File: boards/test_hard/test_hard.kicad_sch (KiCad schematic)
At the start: 12 parts, among them IC1 ADS114S08BIPBS, U2 ESP32-S3-MINI-1

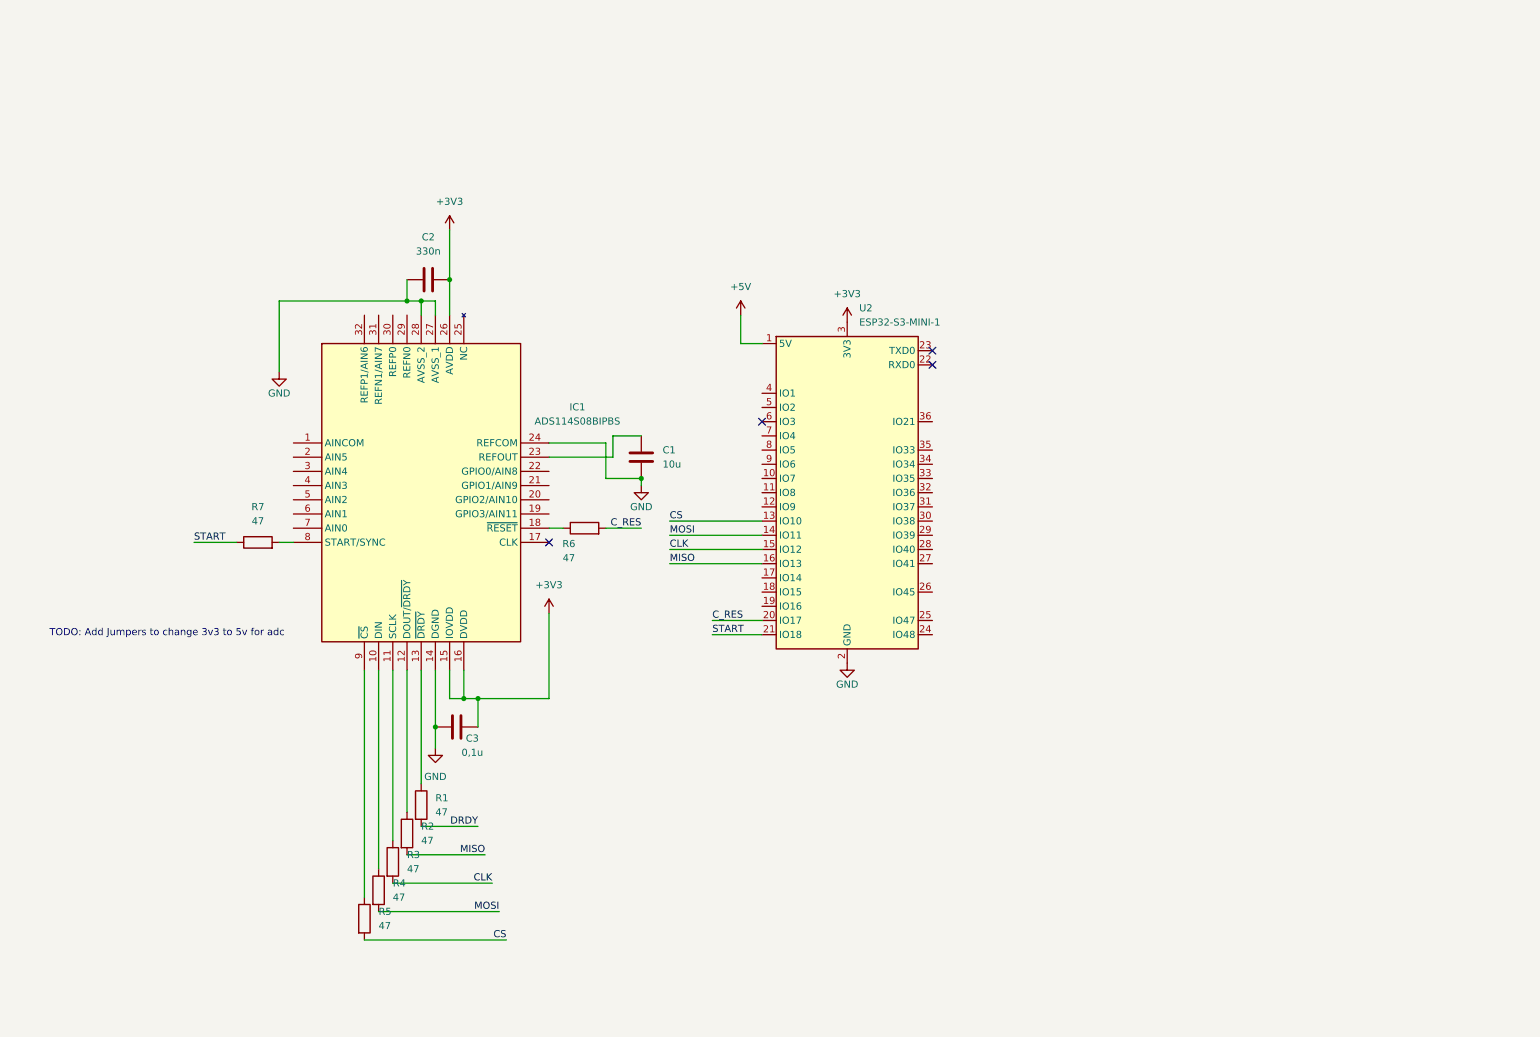
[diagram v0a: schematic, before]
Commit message: Test Hardware Board
Still missing CAN

Signed-off-by: Philipp Macher <philipp-macher@web.de>
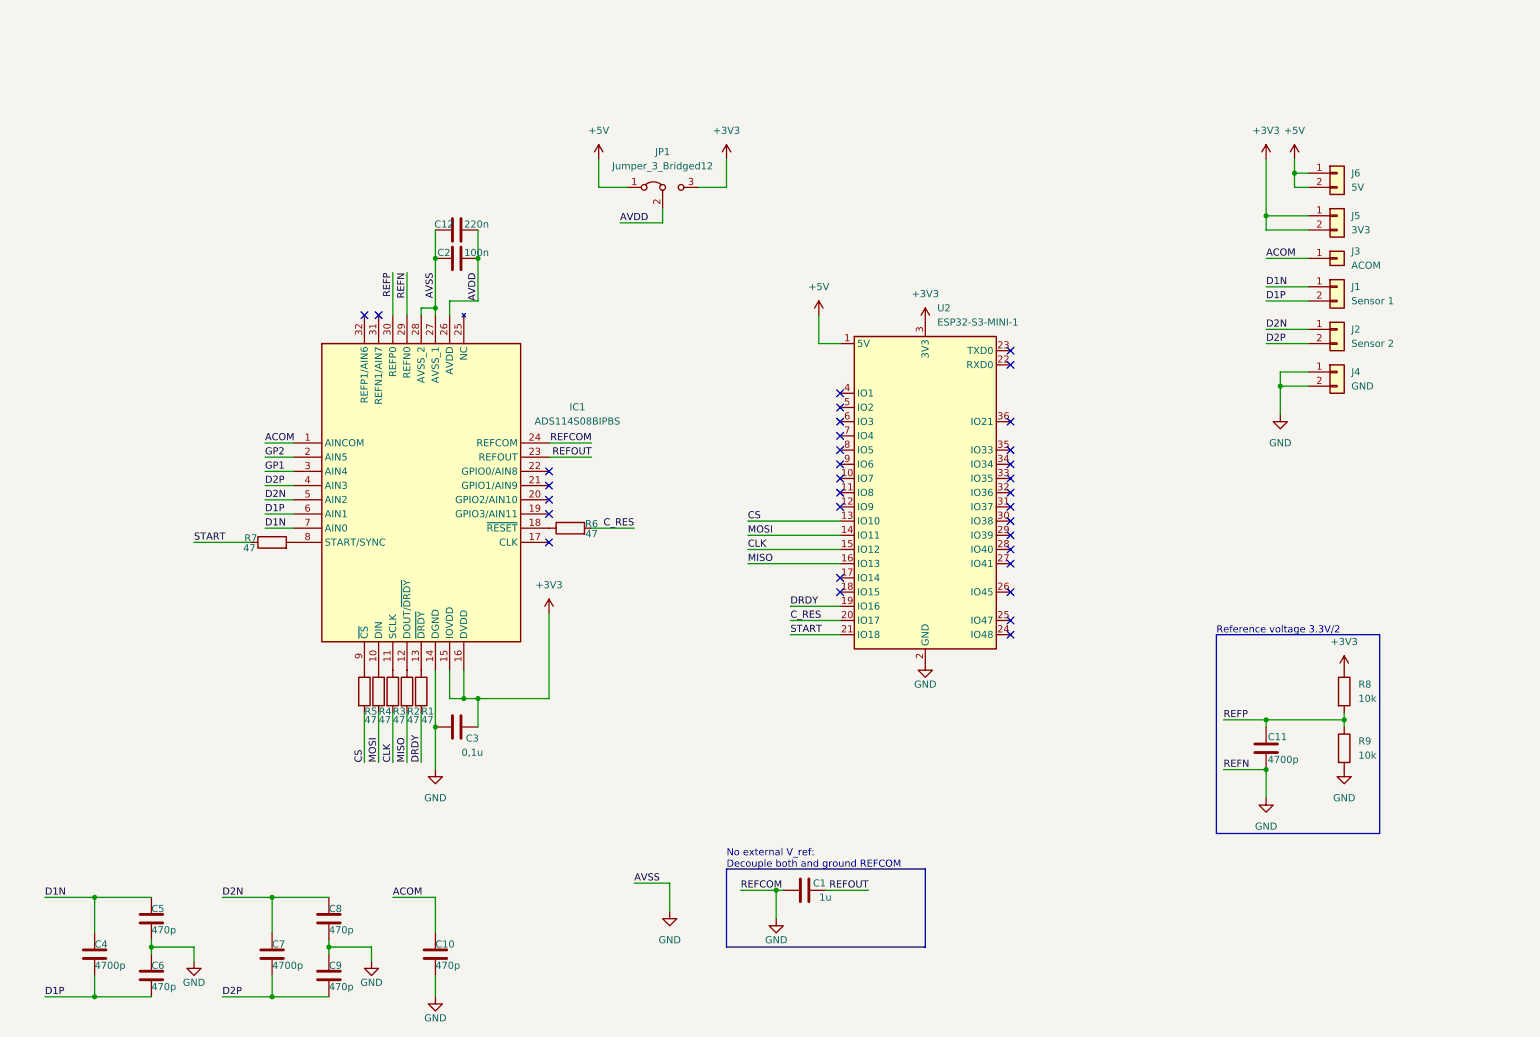
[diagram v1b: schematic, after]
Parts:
- added C10, C5, C6, C8, C9: 470p, Capacitor_SMD:C_0603_1608Metric_Pad1.08x0.95mm_HandSolder, symbol Device:C
- added C11, C4, C7: 4700p, Capacitor_SMD:C_0603_1608Metric_Pad1.08x0.95mm_HandSolder, symbol Device:C
- added C12: 220n, Capacitor_SMD:C_0603_1608Metric_Pad1.08x0.95mm_HandSolder, symbol Device:C
- added J1: Sensor 1, Connector_Wire:SolderWire-0.1sqmm_1x02_P3.6mm_D0.4mm_OD1mm, symbol Connector_Generic:Conn_01x02
- added J2: Sensor 2, Connector_Wire:SolderWire-0.1sqmm_1x02_P3.6mm_D0.4mm_OD1mm, symbol Connector_Generic:Conn_01x02
- added J3: ACOM, Connector_Wire:SolderWire-0.1sqmm_1x01_D0.4mm_OD1mm, symbol Connector_Generic:Conn_01x01
- added J4: GND, Connector_PinHeader_2.54mm:PinHeader_1x02_P2.54mm_Vertical, symbol Connector_Generic:Conn_01x02
- added J5: 3V3, Connector_PinHeader_2.54mm:PinHeader_1x02_P2.54mm_Vertical, symbol Connector_Generic:Conn_01x02
- added J6: 5V, Connector_PinHeader_2.54mm:PinHeader_1x02_P2.54mm_Vertical, symbol Connector_Generic:Conn_01x02
- added JP1: Jumper_3_Bridged12, Connector_PinHeader_2.54mm:PinHeader_1x03_P2.54mm_Vertical, symbol Jumper:Jumper_3_Bridged12
- added R8, R9: 10k, Resistor_SMD:R_0603_1608Metric_Pad0.98x0.95mm_HandSolder, symbol Device:R
- C1: value 10u -> 1u; footprint (none) -> Capacitor_SMD:C_0603_1608Metric_Pad1.08x0.95mm_HandSolder
- C2: value 330n -> 100n; footprint (none) -> Capacitor_SMD:C_0603_1608Metric_Pad1.08x0.95mm_HandSolder
- C3: footprint (none) -> Capacitor_SMD:C_0603_1608Metric_Pad1.08x0.95mm_HandSolder
- R1, R2, R3, R4, R5, R6, R7: footprint (none) -> Resistor_SMD:R_0603_1608Metric_Pad0.98x0.95mm_HandSolder
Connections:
- net +3V3: now also J5.1 (Pin_1), J5.2 (Pin_2), JP1.3 (B), R8.1; no longer C2.2, IC1.26 (AVDD)
- net +5V: now also J6.1 (Pin_1), J6.2 (Pin_2), JP1.1 (A)
- net DRDY: now also U2.19 (IO16)
- net GND: now also C1.2, IC1.29 (REFN0), C10.2, C11.1, C12.1, C5.2, C6.1, C8.2, C9.1, J4.1 (Pin_1), J4.2 (Pin_2), R9.2; no longer C1.1
- net ACOM: now reaches IC1.1 (AINCOM)
- net ACOM: now also C10.1, J3.1 (Pin_1)
- net GP2: now reaches IC1.2 (AIN5)
- net REFOUT: now reaches IC1.23 (REFOUT)
- net REFOUT: now also C1.1; no longer C1.2
- net GP1: now reaches IC1.3 (AIN4)
- net REFP: now reaches IC1.30 (REFP0)
- net REFP: now also C11.2, R8.2, R9.1
- net D2P: now reaches IC1.4 (AIN3)
- net D2P: now also C7.2, C9.2, J2.2 (Pin_2)
- net D2N: now reaches IC1.5 (AIN2)
- net D2N: now also C7.1, C8.1, J2.1 (Pin_1)
- net D1P: now reaches IC1.6 (AIN1)
- net D1P: now also C4.2, C6.2, J1.2 (Pin_2)
- net D1N: now reaches IC1.7 (AIN0)
- net D1N: now also C4.1, C5.1, J1.1 (Pin_1)
- new net AVDD: C12.2, C2.2, IC1.26 (AVDD), JP1.2 (C)
- no-connect marks 4 -> 33
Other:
- note added: "No external V_ref: Decouple both and ground REFCOM"
- note added: "Reference voltage 3.3V/2"
- note removed: "TODO: Add Jumpers to change 3v3 to 5v for adc"
- moved on the sheet: C1, C2, R1, R2, R3, R4, R5, R6, R7, U2

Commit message: Add CAN support to test hardware
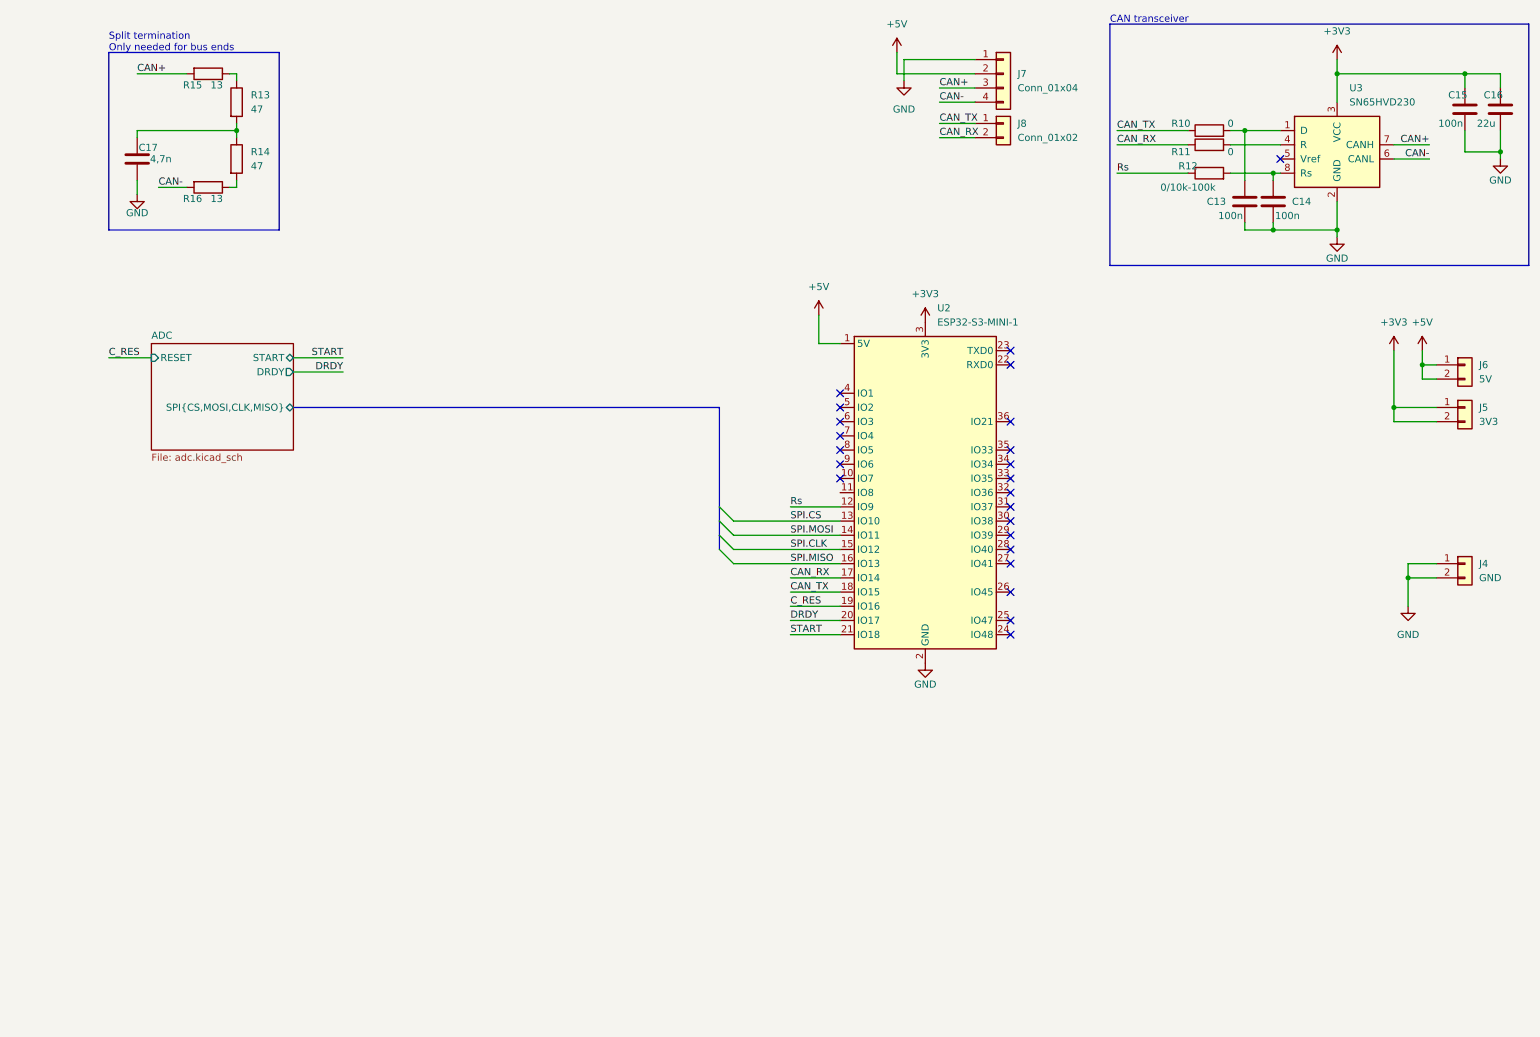
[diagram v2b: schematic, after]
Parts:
- removed C1: 1u, Capacitor_SMD:C_0603_1608Metric_Pad1.08x0.95mm_HandSolder, symbol Device:C
- removed C10, C5, C6, C8, C9: 470p, Capacitor_SMD:C_0603_1608Metric_Pad1.08x0.95mm_HandSolder, symbol Device:C
- removed C11, C4, C7: 4700p, Capacitor_SMD:C_0603_1608Metric_Pad1.08x0.95mm_HandSolder, symbol Device:C
- removed C12: 220n, Capacitor_SMD:C_0603_1608Metric_Pad1.08x0.95mm_HandSolder, symbol Device:C
- removed C2: 100n, Capacitor_SMD:C_0603_1608Metric_Pad1.08x0.95mm_HandSolder, symbol Device:C
- removed C3: 0,1u, Capacitor_SMD:C_0603_1608Metric_Pad1.08x0.95mm_HandSolder, symbol Device:C
- removed IC1: ADS114S08BIPBS, ADS114S08BIPBS:QFP50P700X700X120-32N, symbol ADS114S08BIPBS:ADS114S08BIPBS
- removed J1: Sensor 1, Connector_Wire:SolderWire-0.1sqmm_1x02_P3.6mm_D0.4mm_OD1mm, symbol Connector_Generic:Conn_01x02
- removed J2: Sensor 2, Connector_Wire:SolderWire-0.1sqmm_1x02_P3.6mm_D0.4mm_OD1mm, symbol Connector_Generic:Conn_01x02
- removed J3: ACOM, Connector_Wire:SolderWire-0.1sqmm_1x01_D0.4mm_OD1mm, symbol Connector_Generic:Conn_01x01
- removed JP1: Jumper_3_Bridged12, Connector_PinHeader_2.54mm:PinHeader_1x03_P2.54mm_Vertical, symbol Jumper:Jumper_3_Bridged12
- removed R1, R2, R3, R4, R5, R6, R7: 47, Resistor_SMD:R_0603_1608Metric_Pad0.98x0.95mm_HandSolder, symbol Device:R
- removed R8, R9: 10k, Resistor_SMD:R_0603_1608Metric_Pad0.98x0.95mm_HandSolder, symbol Device:R
- added C13, C14, C15: 100n, Capacitor_SMD:C_0603_1608Metric_Pad1.08x0.95mm_HandSolder, symbol Device:C
- added C16: 22u, Capacitor_SMD:C_0603_1608Metric_Pad1.08x0.95mm_HandSolder, symbol Device:C
- added C17: 4,7n, Capacitor_SMD:C_0603_1608Metric_Pad1.08x0.95mm_HandSolder, symbol Device:C
- added J7: Conn_01x04, TerminalBlock:TerminalBlock_bornier-4_P5.08mm, symbol Connector_Generic:Conn_01x04
- added J8: Conn_01x02, Connector_PinHeader_2.54mm:PinHeader_1x02_P2.54mm_Vertical, symbol Connector_Generic:Conn_01x02
- added R10, R11: 0, Resistor_SMD:R_0603_1608Metric_Pad0.98x0.95mm_HandSolder, symbol Device:R
- added R12: 0/10k-100k, Resistor_SMD:R_0603_1608Metric_Pad0.98x0.95mm_HandSolder, symbol Device:R
- added R13, R14: 47, Resistor_SMD:R_0603_1608Metric_Pad0.98x0.95mm_HandSolder, symbol Device:R
- added R15, R16: 13, Resistor_SMD:R_0603_1608Metric_Pad0.98x0.95mm_HandSolder, symbol Device:R
- added U3: SN65HVD230, Package_SO:SOIC-8_3.9x4.9mm_P1.27mm, symbol Interface_CAN_LIN:SN65HVD230
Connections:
- net +3V3: now also C15.1, C16.1, U3.3 (VCC)
- net +5V: now also J7.2 (Pin_2)
- net C_RES: now also U2.19 (IO16); no longer U2.20 (IO17)
- net DRDY: now also U2.20 (IO17); no longer U2.19 (IO16)
- net GND: now also C13.2, C14.2, C15.2, C16.2, C17.2, J7.1 (Pin_1), U3.2 (GND)
- net Rs: now reaches U2.12 (IO9)
- net Rs: now also R12.1
- net CAN_RX: now reaches U2.17 (IO14)
- net CAN_RX: now also J8.2 (Pin_2), R11.1
- net CAN_TX: now reaches U2.18 (IO15)
- net CAN_TX: now also J8.1 (Pin_1), R10.1
- net CLK renamed SPI.CLK
- net CS renamed SPI.CS
- net MISO renamed SPI.MISO
- net MOSI renamed SPI.MOSI
- new net: R13.1, R15.1
- new net: C17.1, R13.2, R14.1
- new net: R11.2, U3.4 (R)
- new net: C13.1, R10.2, U3.1 (D)
- new net: C14.1, R12.2, U3.8 (Rs)
- new net: R14.2, R16.1
- new net CAN+: J7.3 (Pin_3), R15.2, U3.7 (CANH)
- new net CAN-: J7.4 (Pin_4), R16.2, U3.6 (CANL)
- no-connect marks 33 -> 23
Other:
- added sheet ADC (adc.kicad_sch)
- note added: "CAN transceiver"
- note added: "Split termination Only needed for bus ends"
- note removed: "No external V_ref: Decouple both and ground REFCOM"
- note removed: "Reference voltage 3.3V/2"
- moved on the sheet: J4, J5, J6

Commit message: Aktueller Stand
Signed-off-by: Philipp Macher <philipp-macher@web.de>
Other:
- moved on the sheet: J4, J5, J6, J7, J8, U2
